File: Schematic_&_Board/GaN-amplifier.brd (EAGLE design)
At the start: 120.7 x 50.8 mm, 114 parts, among them IC1 LT3080, J1 JOHNSON_SMA_EDGE_LAUNCH_142-0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, J2 JOHNSON_SMA_EDGE_LAUNCH_142-0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, Q1 MMBT3906LT1SMD, T1 IPB080N03L G, T2 IPB080N03L G, T3 IPB080N03L G, T4 IPB080N03L G, T5 BSP89, U1 TPS7A30XX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

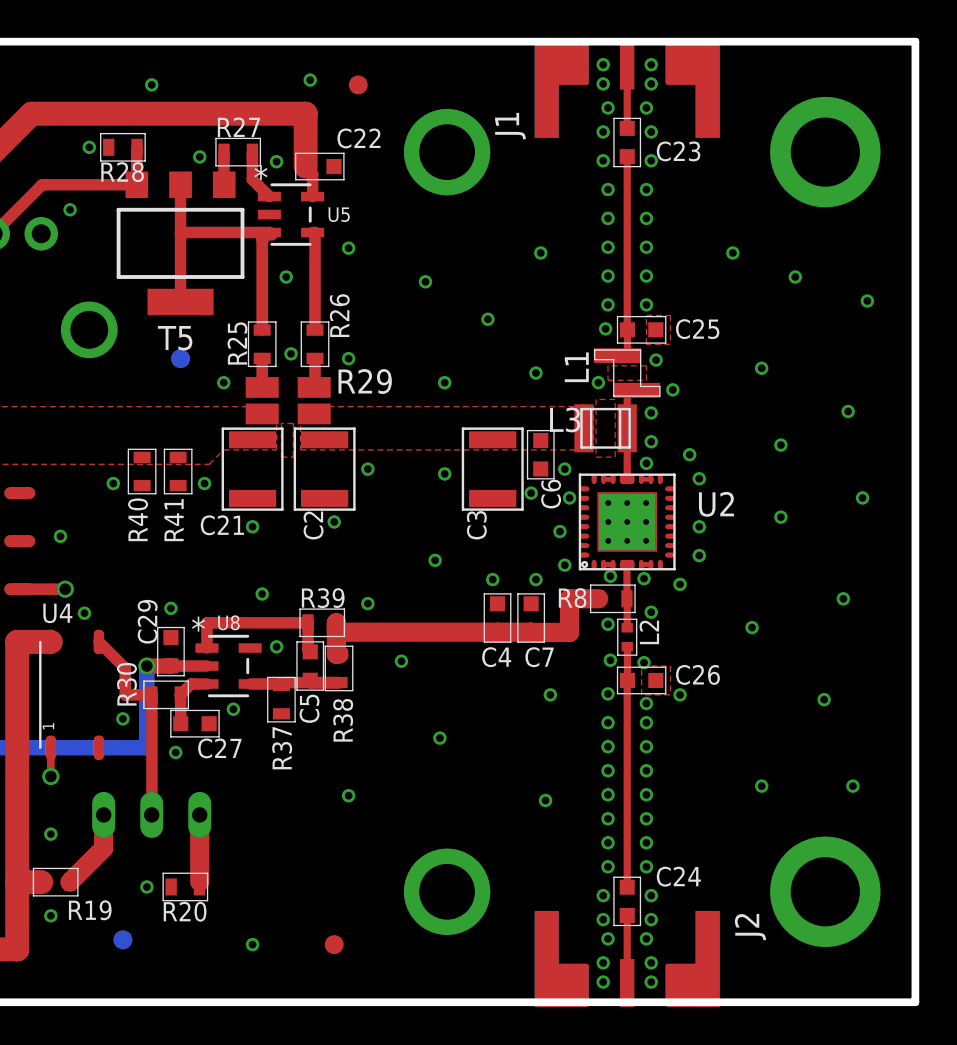
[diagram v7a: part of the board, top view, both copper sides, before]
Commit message: Enlarging heatsink pad
Enlarging the pad for the backside heatsink and adding vias for better
power dissipation.

DSB
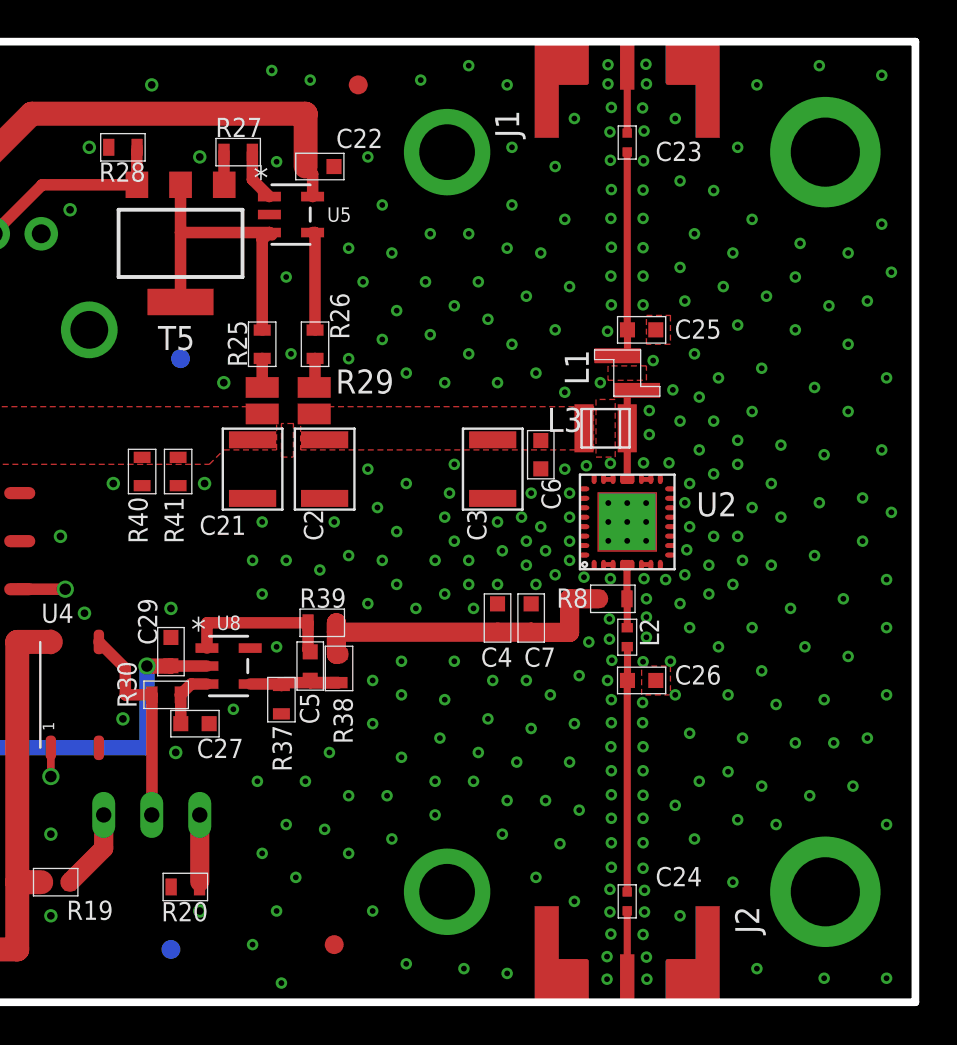
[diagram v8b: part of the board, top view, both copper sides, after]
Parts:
- C23, C24: value 10n -> 100n; device jqi_passives:C_MLCC_0603 -> jqi_passives:C_MLCC_0402
- moved FID8 2.59 mm to (81.3, 2.79)
- moved J2 0.25 mm to (105.4, 0.00)
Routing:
- net GND: vias 194 -> 378
